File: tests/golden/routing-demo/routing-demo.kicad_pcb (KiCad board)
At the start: 2 copper layers, 40 x 56 mm, 6 parts, among them J1 CONN_ISP_1X06, U1 ATTINY85_DIP8

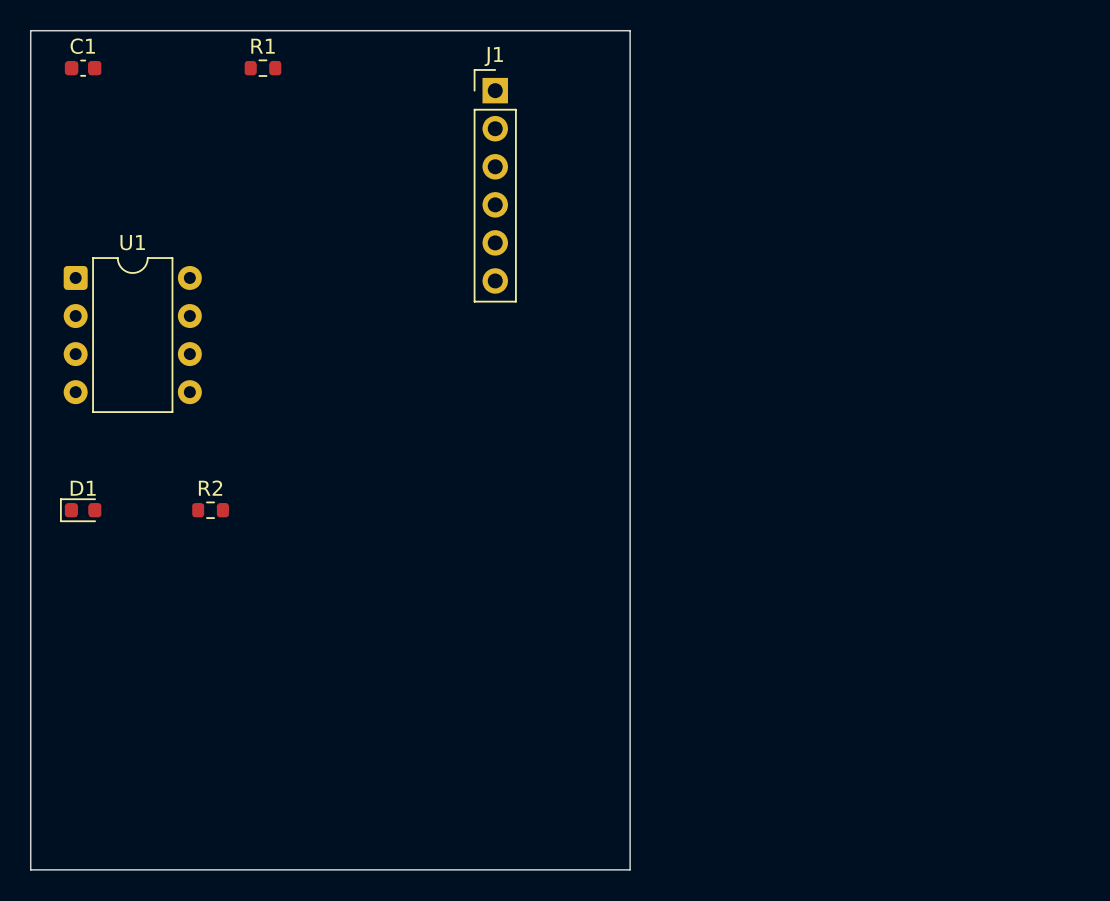
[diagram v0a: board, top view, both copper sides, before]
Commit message: M7a+M7b: topological routing — sketches in source, DRC-clean copper out
Routes are stored as topology: which obstacles a wire passes and on which side.
Nothing in the source is a coordinate, so moving a part leaves the sketch true and
only the tightening re-runs — which is the whole point of the approach (ADR 0006,
written after reading SURF, Maley, TopoR and the shortest-homotopic-path
literature).

Geometry comes from the classical pipeline: inflate obstacles by the clearance the
net needs, triangulate what is left (constrained Delaunay, via Shapely/GEOS), turn
the sketch into a crossing sequence, reduce it to a canonical homotopy class, and
tighten the resulting sleeve with the funnel algorithm. Inflating first is what
makes the shortest path automatically a legal one.

All four examples route with **zero DRC violations and zero schematic-parity
issues**; ldo-supply routes completely, 13 of 13 connections with nothing
unconnected. Unroutable connections are reported with a reason.

Almost every defect here was invisible to structural checks — the sleeve stayed
valid, the funnel still terminated, and the board was still legal. Each was found by
measuring the result:

* portal orientation had the wrong sign for Y-down board coordinates, turning a
  24.6 mm route into a 162.6 mm zigzag between the pad rows.
* searching triangle centroids instead of portal midpoints sent routes to the board
  corner and back, because a CDT of sparse obstacles has a few enormous triangles.
* an A* node has to be a *crossing*, not a diagonal: keyed on the diagonal alone the
  search steps through one without crossing it.
* feeding a finished route back as one convex hull swallowed the area inside every
  bend, costing a third of the connections.
* track obstacles pre-inflated by the routed net's own half-width left every later
  track short by half of its own, exactly as DRC reported.
* KiCad enforces the larger of two nets' clearances, not the routing net's.
* four shield tabs sharing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
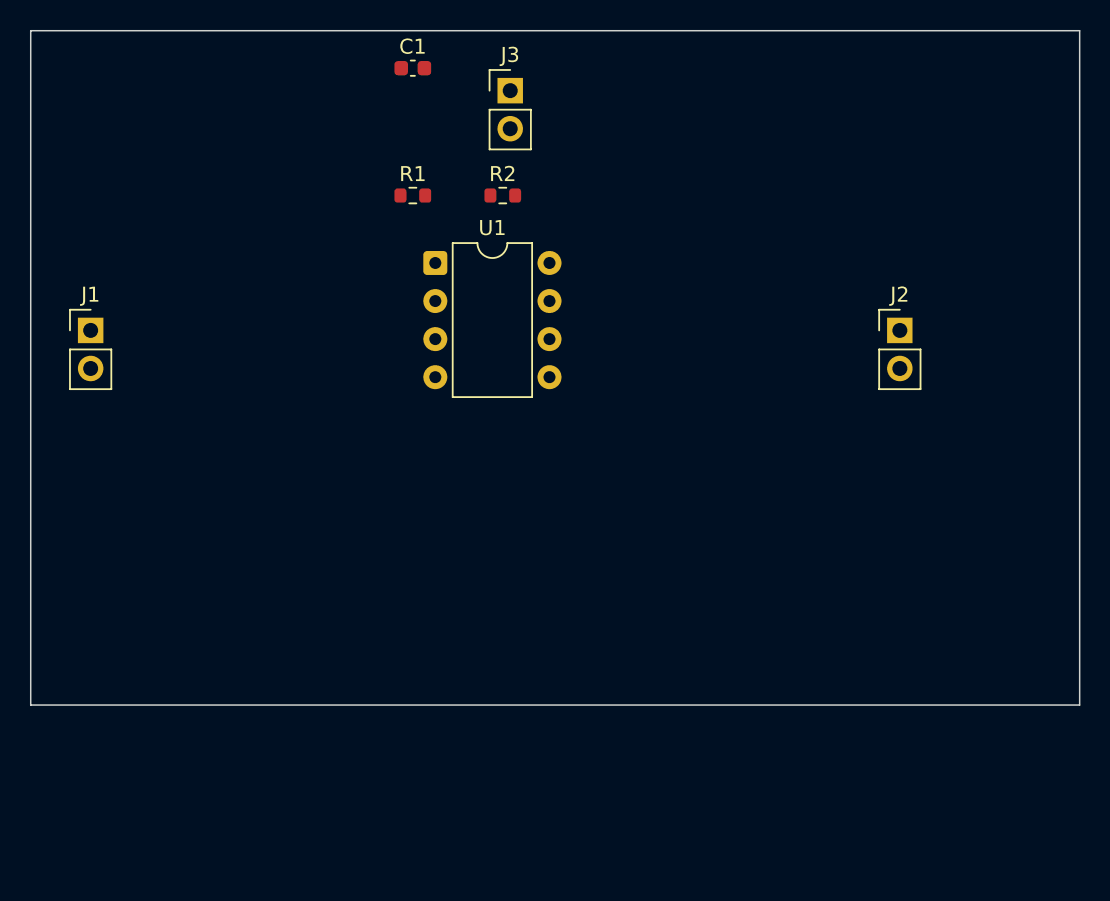
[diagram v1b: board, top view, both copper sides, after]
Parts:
- removed D1: LED_RED_0603, LED_SMD:LED_0603_1608Metric
- added J2: CONN_PWR_1X02, Connector_PinHeader_2.54mm:PinHeader_1x02_P2.54mm_Vertical, F.Cu at (158.0, 120.0)
- added J3: CONN_PWR_1X02, Connector_PinHeader_2.54mm:PinHeader_1x02_P2.54mm_Vertical, F.Cu at (132.0, 104.0)
- J1: value CONN_ISP_1X06 -> CONN_PWR_1X02; footprint Connector_PinHeader_2.54mm:PinHeader_1x06_P2.54mm_Vertical -> Connector_PinHeader_2.54mm:PinHeader_1x02_P2.54mm_Vertical
- R2: value R_330R_0603 -> R_10K_0603
- moved J1 31.4 mm to (104.0, 120.0)
- moved R2 28.7 mm to (131.5, 111.0)
- moved U1 24.0 mm to (127.0, 115.5)
- moved C1 22.0 mm to (125.5, 102.5)
- moved R1 13.1 mm to (125.5, 111.0)
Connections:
- J1 pad 1: PB1 -> CROSS
- J1 pad 2: VCC -> GND
- R2 pad 1: PB4 -> RESET
- R2 pad 2: led1.ANODE -> SENSE
- U1 pad 1: RESET -> unconnected-(U1-~{RESET}/PB5-Pad1)
- U1 pad 3: PB4 -> unconnected-(U1-XTAL2/PB4-Pad3)
- U1 pad 5: PB0 -> unconnected-(U1-AREF/PB0-Pad5)
- U1 pad 6: PB1 -> SENSE
- U1 pad 7: PB2 -> unconnected-(U1-PB2-Pad7)
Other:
- board size 40 x 56 mm -> 70 x 45 mm
